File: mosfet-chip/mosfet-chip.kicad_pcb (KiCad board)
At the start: 2 copper layers, 33.7 x 17.1 mm, 10 parts, among them J1 Conn_01x02, J2 Screw_Terminal_01x02, J3 Screw_Terminal_01x02, Q1 IRLZ34

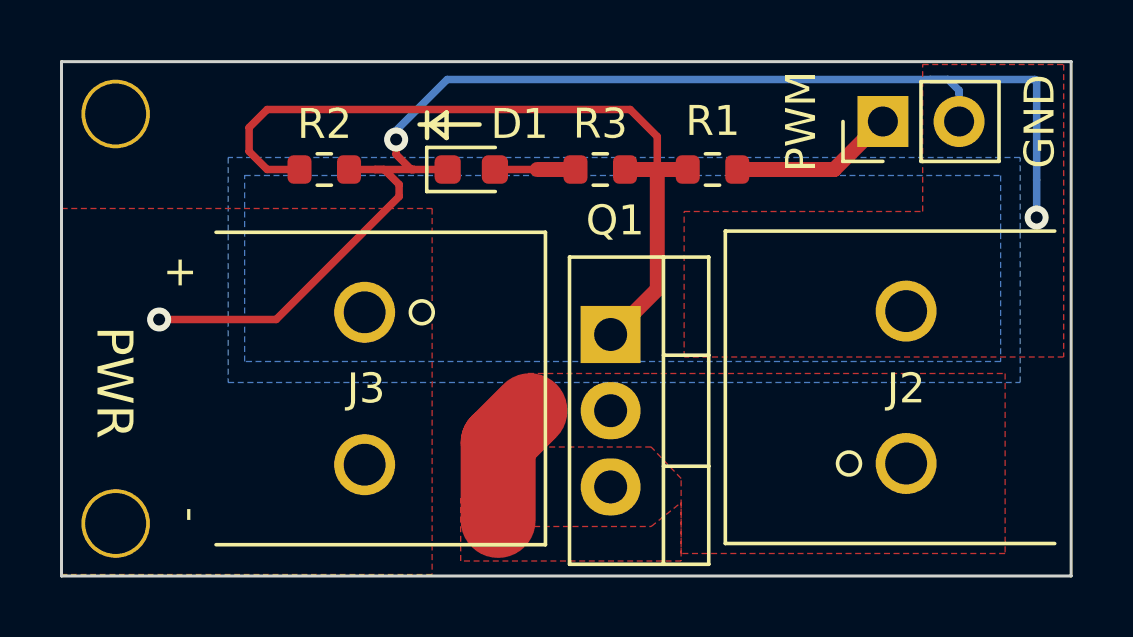
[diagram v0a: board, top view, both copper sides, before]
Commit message: Move traces to more gracefully handle mouse bites
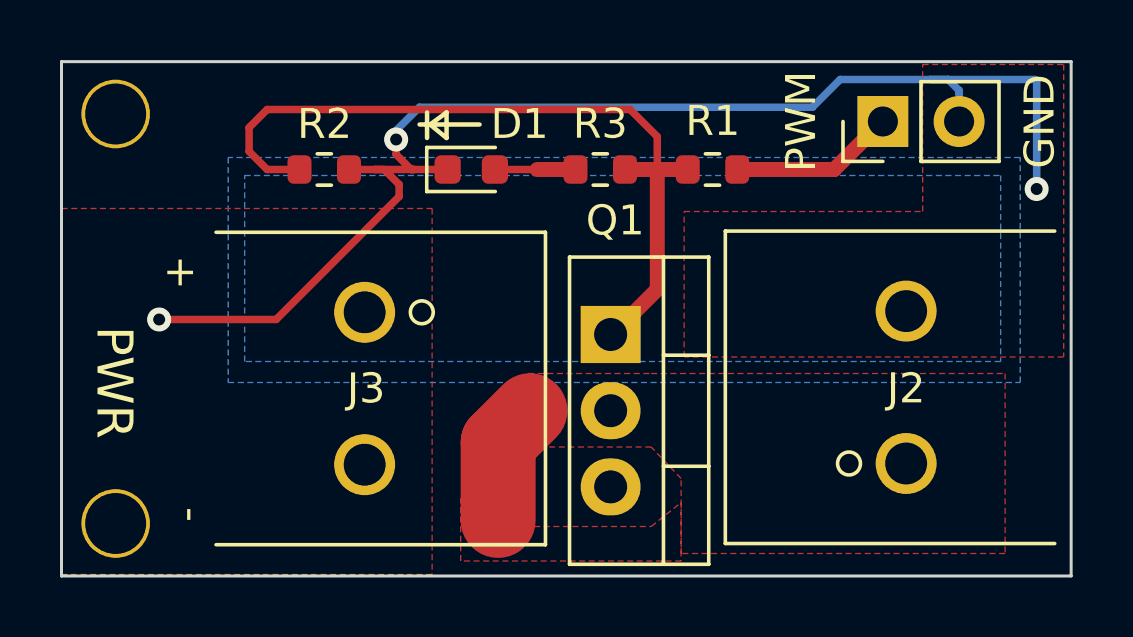
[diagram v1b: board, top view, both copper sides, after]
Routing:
- net GND: track 44.8 -> 43.8 mm
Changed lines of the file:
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@@
   (segment (start 65.1 62.1) (end 65.1 61.7) (width 0.25) (layer "F.Cu") (net 1))
   (via (at 57.1 66.2) (size 0.8) (drill 0.4) (layers "F.Cu" "B.Cu") (free) (net 1))
-  (via (at 86.35 62.8) (size 0.8) (drill 0.4) (layers "F.Cu" "B.Cu") (free) (net 1))
+  (via (at 86.35 61.85) (size 0.8) (drill 0.4) (layers "F.Cu" "B.Cu") (free) (net 1))
   (via (at 65 60.2) (size 0.8) (drill 0.4) (layers "F.Cu" "B.Cu") (net 1))
+  (segment (start 82.8 58.2) (end 79.8 58.2) (width 0.25) (layer "B.Cu") (net 1))
   (segment (start 83.4 58.2) (end 83.765 58.565) (width 0.25) (layer "B.Cu") (net 1))
+  (segment (start 65.775 59.125) (end 65 59.9) (width 0.25) (layer "B.Cu") (net 1))
   (segment (start 83.765 58.565) (end 83.765 58.665) (width 0.25) (layer "B.Cu") (net 1))
-  (segment (start 86.3 58.2) (end 86.35 58.25) (width 0.25) (layer "B.Cu") (net 1))
-  (segment (start 82.8 58.2) (end 66.7 58.2) (width 0.25) (layer "B.Cu") (net 1))
-  (segment (start 65 59.9) (end 66.7 58.2) (width 0.25) (layer "B.Cu") (net 1))
   (segment (start 83.765 59.6) (end 83.765 58.665) (width 0.25) (layer "B.Cu") (net 1))
-  (segment (start 82.8 58.2) (end 86.3 58.2) (width 0.25) (layer "B.Cu") (net 1))
-  (segment (start 86.35 58.25) (end 86.35 61.55) (width 0.25) (layer "B.Cu") (net 1))
-  (segment (start 65 60.2) (end 65 59.9) (width 0.25) (layer "B.Cu") (net 1))
+  (segment (start 86.3 58.2) (end 82.8 58.2) (width 0.25) (layer "B.Cu") (net 1))
+  (segment (start 79.8 58.2) (end 78.875 59.125) (width 0.25) (layer "B.Cu") (net 1))
+  (segment (start 86.35 58.25) (end 86.3 58.2) (width 0.25) (layer "B.Cu") (net 1))
+  (segment (start 86.35 61.85) (end 86.35 58.25) (width 0.25) (layer "B.Cu") (net 1))
+  (segment (start 78.875 59.125) (end 65.775 59.125) (width 0.25) (layer "B.Cu") (net 1))
   (segment (start 83.4 58.2) (end 82.8 58.2) (width 0.25) (layer "B.Cu") (net 1))
-  (segment (start 86.35 62.8) (end 86.35 61.55) (width 0.25) (layer "B.Cu") (net 1))
+  (segment (start 65 59.9) (end 65 60.2) (width 0.25) (layer "B.Cu") (net 1))
   (segment (start 79.6 61.2) (end 76.37 61.2) (width 0.5) (layer "F.Cu") (net 2))
   (segment (start 81.2 59.6) (end 79.6 61.2) (width 0.5) (layer "F.Cu") (net 2))

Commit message: Small routed fillet on corners.
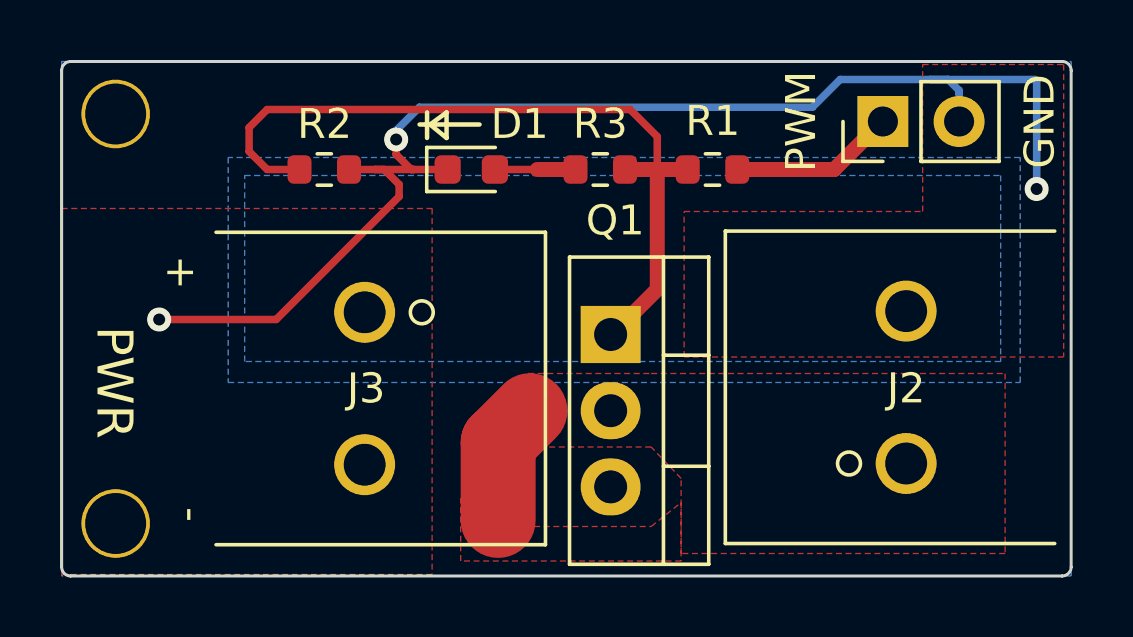
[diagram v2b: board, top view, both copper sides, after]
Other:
- board size 33.7 x 17.1 mm -> 33.6 x 17.1 mm
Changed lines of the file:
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@@
   (gr_line (start 66.13 59.7) (end 66.68 59.3) (layer "F.SilkS") (width 0.15))
   (gr_line (start 66.13 59.7) (end 66.68 60.15) (layer "F.SilkS") (width 0.15))
-  (gr_rect locked (start 53.845003 57.60499) (end 87.500003 74.74999) (layer "Edge.Cuts") (width 0.1) (fill none))
+  (gr_line (start 54.15 74.75) (end 87.2 74.75) (layer "Edge.Cuts") (width 0.1))
+  (gr_line (start 53.85 57.9) (end 53.85 74.45) (layer "Edge.Cuts") (width 0.1))
+  (gr_line (start 87.2 57.6) (end 54.15 57.6) (layer "Edge.Cuts") (width 0.1))
+  (gr_arc (start 87.5 74.45) (mid 87.412132 74.662132) (end 87.2 74.75) (layer "Edge.Cuts") (width 0.1))
+  (gr_line (start 87.5 74.45) (end 87.5 57.9) (layer "Edge.Cuts") (width 0.1))
+  (gr_arc (start 53.85 57.9) (mid 53.937868 57.687868) (end 54.15 57.6) (layer "Edge.Cuts") (width 0.1))
+  (gr_arc (start 87.2 57.6) (mid 87.412132 57.687868) (end 87.5 57.9) (layer "Edge.Cuts") (width 0.1))
+  (gr_arc (start 54.15 74.75) (mid 53.937868 74.662132) (end 53.85 74.45) (layer "Edge.Cuts") (width 0.1))
   (gr_text "${board_name}" (at 74.2 62.4) (layer "B.SilkS")
     (effects (font (size 1 1) (thickness 0.15)) (justify mirror))
